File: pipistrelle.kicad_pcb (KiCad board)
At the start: 2 copper layers, 38 x 100 mm, 69 parts, among them J1 C2M, J2 C2F, J3 Eurorack Power, J4 CV1, J5 V/OCT, J6 OUT, J7 CV2, J8 C1M, J9 C1F, U1 SeeeduinoXIAO, U2 MCP6002-xSN, U3 MCP6002-xSN, U4 TL072, U5 LM1117-5.0, U6 LM4040DBZ-10

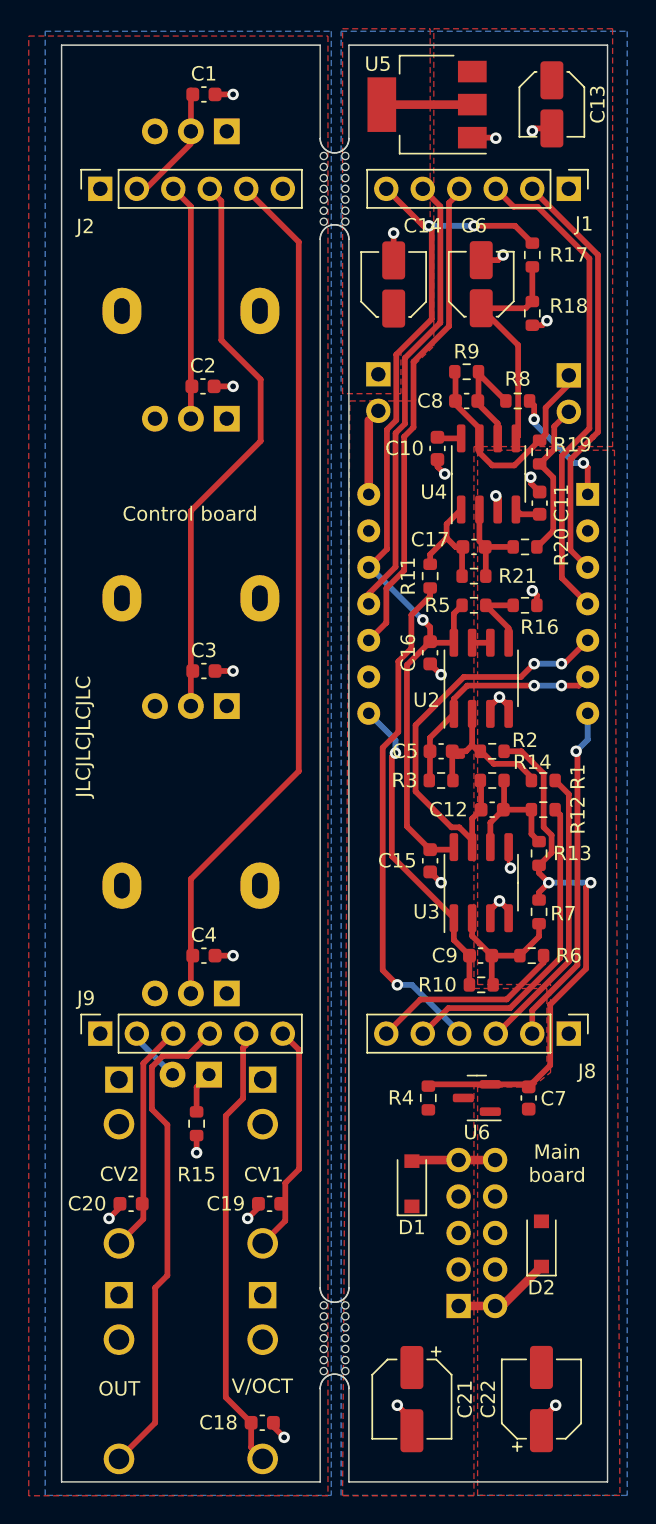
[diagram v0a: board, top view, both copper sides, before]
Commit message: Use 1k for LED resistor
Tested, and plenty bright enough.
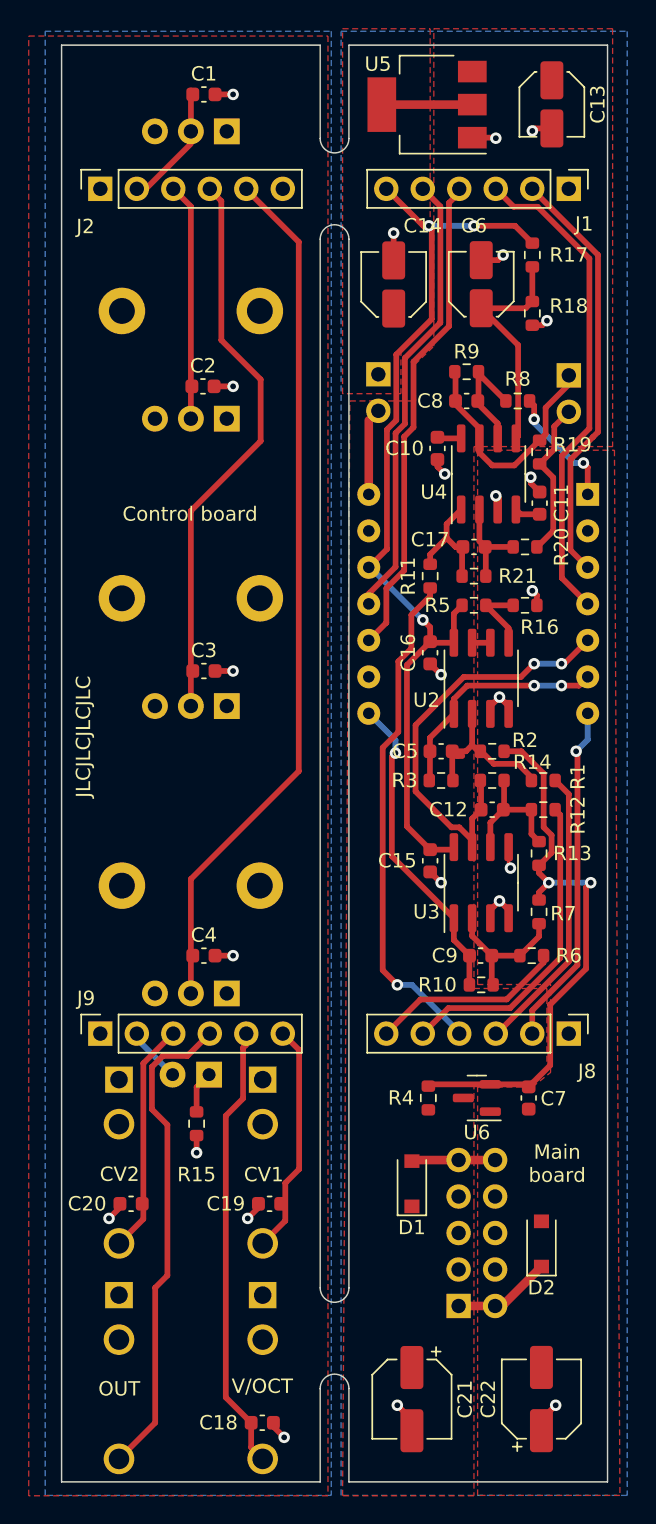
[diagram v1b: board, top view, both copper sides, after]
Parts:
- removed mouse-bite-2x5mm (x2): VAL**, Personal:Mouse_bite_2x5mm
- R15: value 68 -> 1k

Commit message: Update footprints
Mouse bites are now in the schematic so they won't disappear on update
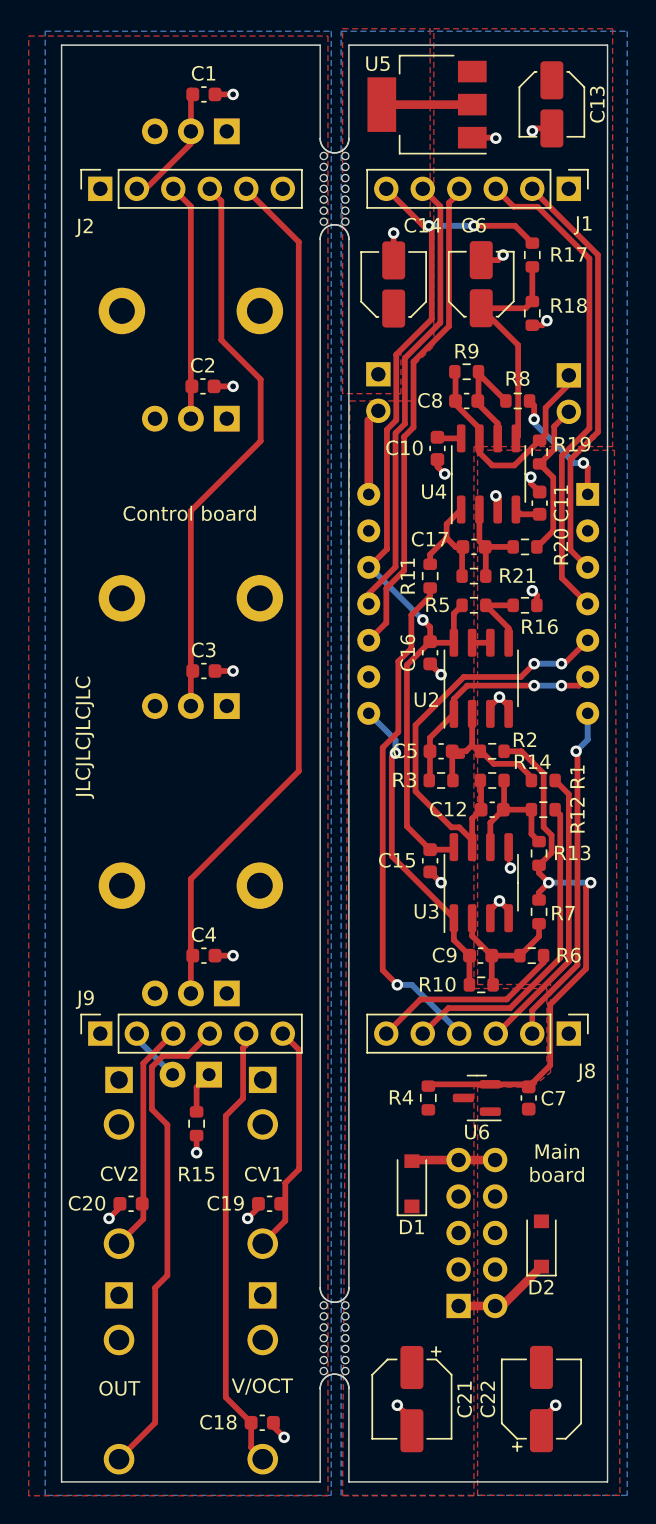
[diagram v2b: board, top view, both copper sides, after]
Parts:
- added H1: Mousebite, Personal:Mouse_bite_2x5mm, F.Cu at (169.0, 140.0)
- added H2: Mousebite, Personal:Mouse_bite_2x5mm, F.Cu at (169.0, 60.0)
- moved RV1 7.91 mm to (159.0, 48.5), turned to 180 degrees
- moved RV2 7.91 mm to (159.0, 68.5), turned to 180 degrees
- moved RV3 7.91 mm to (159.0, 88.5), turned to 180 degrees
- moved RV4 7.91 mm to (159.0, 108.5), turned to 180 degrees
- moved J4 6.50 mm to (164.0, 128.5)
- moved J5 6.50 mm to (164.0, 143.5)
- moved J6 6.50 mm to (154.0, 143.5)
- moved J7 6.50 mm to (154.0, 128.5)

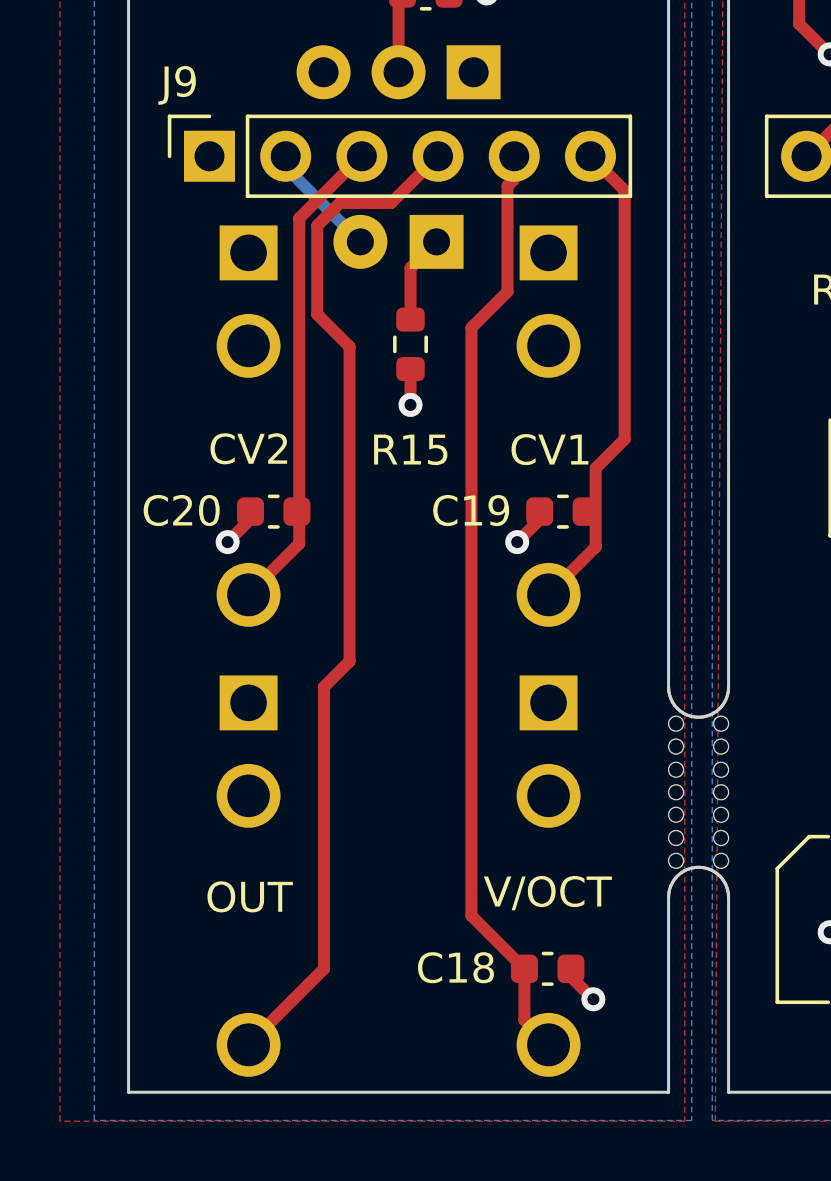
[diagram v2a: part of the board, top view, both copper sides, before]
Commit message: Change ESD cap to 1206
The 0603 I intended to use is unavailable at JLC, and there's plenty of
space.
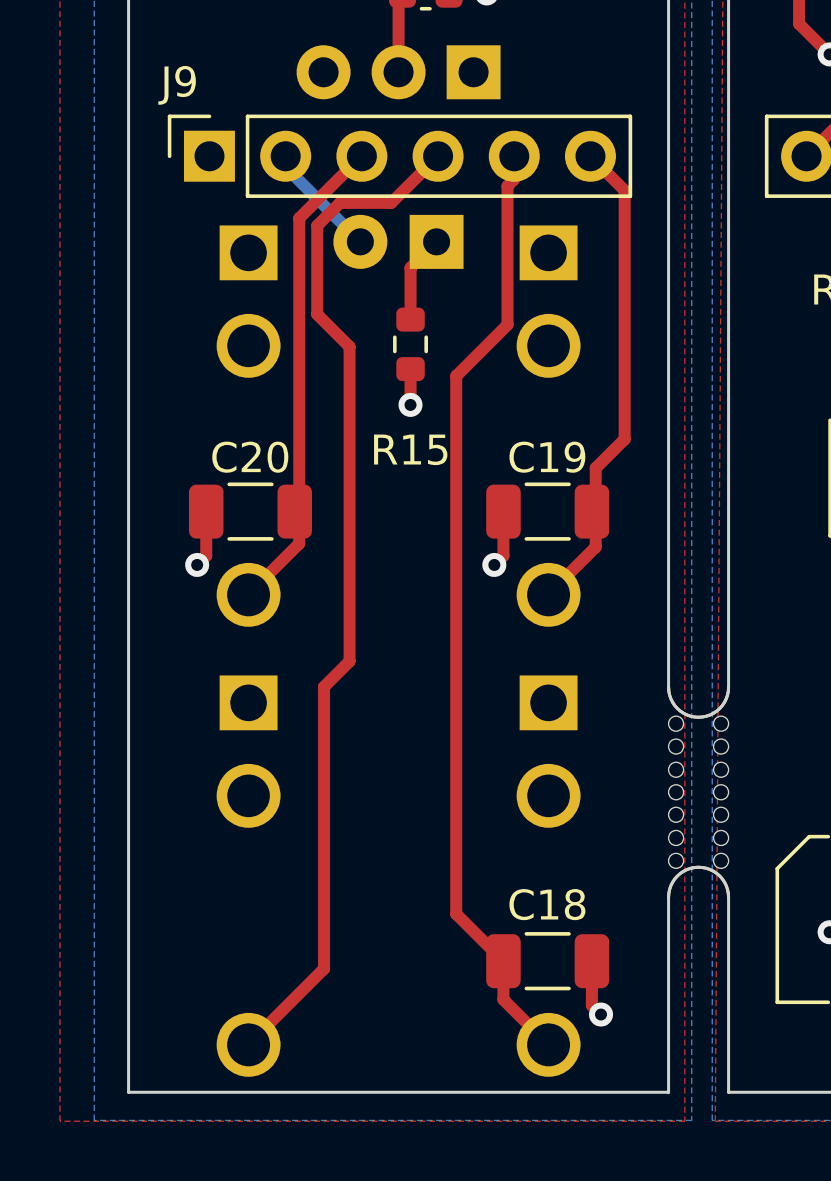
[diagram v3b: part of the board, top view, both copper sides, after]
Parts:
- C18, C19, C20: footprint Capacitor_SMD:C_0603_1608Metric -> Capacitor_SMD:C_1206_3216Metric
- moved C20 0.77 mm to (154.1, 130.6)
- moved C19 0.51 mm to (164.0, 130.6)
- moved C18 0.25 mm to (164.0, 145.6)
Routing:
- net GND1: track 10.3 -> 12.0 mm
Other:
- board text removed: "CV1"
- board text removed: "CV2"
- board text removed: "OUT"
- board text removed: "V/OCT"

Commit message: Use ABCD for pot designations as front panel
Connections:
- net /CONN_POT1 renamed /CONN_POTD
- net /CONN_POT2 renamed /CONN_POTC
- net /CONN_POT3 renamed /CONN_POTB
- net /CONN_POT4 renamed /CONN_POTA
- net /POT1_IN renamed /POTD_IN
- net /POT2_IN renamed /POTC_IN
- net /POT3_IN renamed /POTB_IN
- net /POT4_IN renamed /POTA_IN

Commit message: Use more common values for offset divider
Neither 110 nor 300 are E12, but 100 is E6.
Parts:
- R17: value 330k -> 300k
- R18: value 200k -> 100k
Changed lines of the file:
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@@
       (effects (font (size 1 1) (thickness 0.15)))
     )
-    (fp_text value "200k" (at 0 1.43 90) (layer "F.Fab")
+    (fp_text value "100k" (at 0 1.43 90) (layer "F.Fab")
       (effects (font (size 1 1) (thickness 0.15)))
     )
@@
       (effects (font (size 1 1) (thickness 0.15)))
     )
-    (fp_text value "330k" (at 0 1.43 90) (layer "F.Fab")
+    (fp_text value "300k" (at 0 1.43 90) (layer "F.Fab")
       (effects (font (size 1 1) (thickness 0.15)))
     )
